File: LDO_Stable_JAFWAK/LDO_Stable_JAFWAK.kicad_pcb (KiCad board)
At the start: 4 copper layers, 96.5 x 51.1 mm, 79 parts, among them J1 VDD_SEL, J10 Load Cell and Buffer, J11 GND, J12 GND, J13 AD_PINS, J2 EN_FG, J3 VIN_FG, J4 VS_BUFF, J5 VOUT, J6 EN_AIN_SEL, J7 VIN_DC, J8 EN_SEL, J9 VOUT_BUFF, Q1 FDV305N, Q2 FDV305N, Q3 FDV305N, Q4 FDV305N, Q5 FDV305N, U1 SU272AFJK_LDO, U2 BUF634AIDR, U3 TMP235A2DBZR, U4 BUF634AIDR, U5 FXLP34, U6 FXLP34

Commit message: Produced Gerbers
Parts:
- added G***: LOGO, TPS7A7001_Evaluation_Board_footprint_lib:Stanford_logo, F.Cu at (94.0, 105.2)
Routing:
- net INB: track 69.4 -> 70.3 mm
- added copper zone on B.Cu, net GND
- added copper zone on F.Cu, net GND
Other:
- board size 96.5 x 51.1 mm -> 98.8 x 51.1 mm
- board text added: "JAFWAK"
- board text added: "Joseph Khamisy"
- board text removed: "Joseph Khamiby"

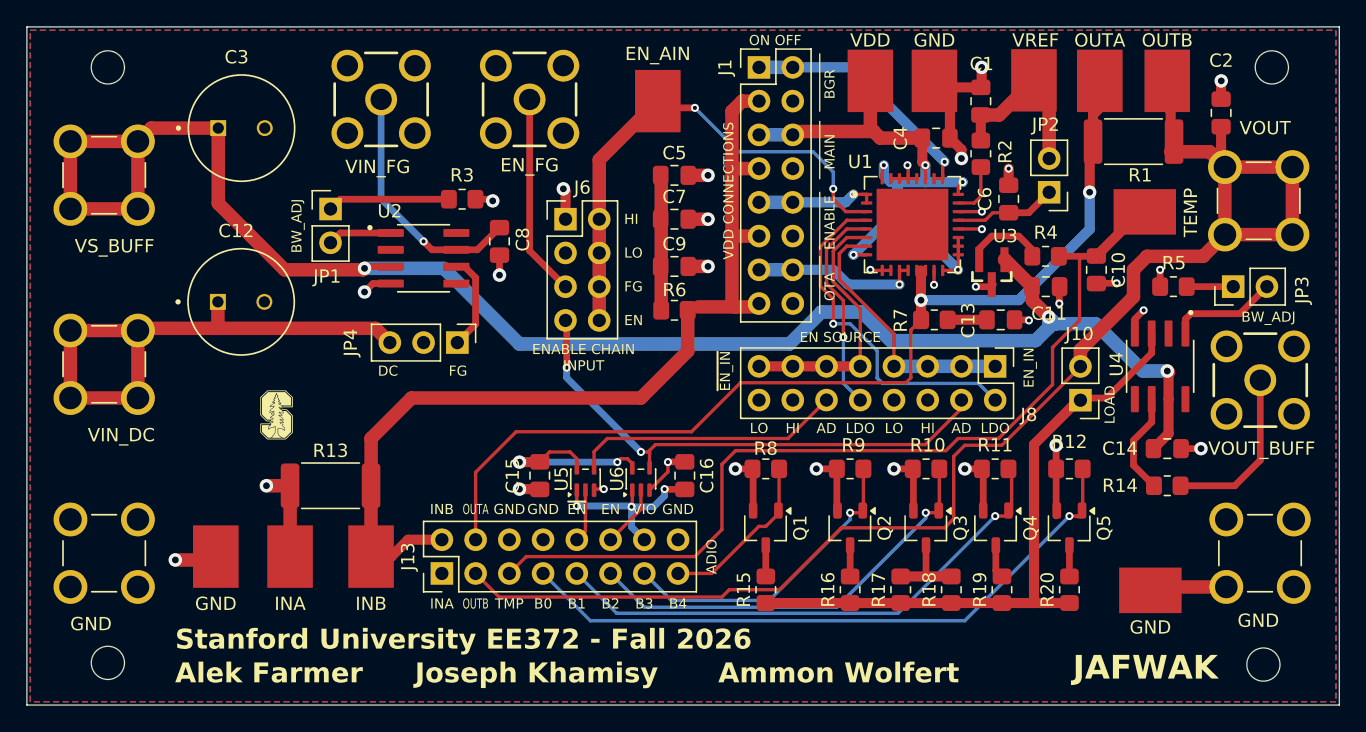
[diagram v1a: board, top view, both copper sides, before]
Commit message: Couple changes
More caps
Series Resitors
Stiching Vias
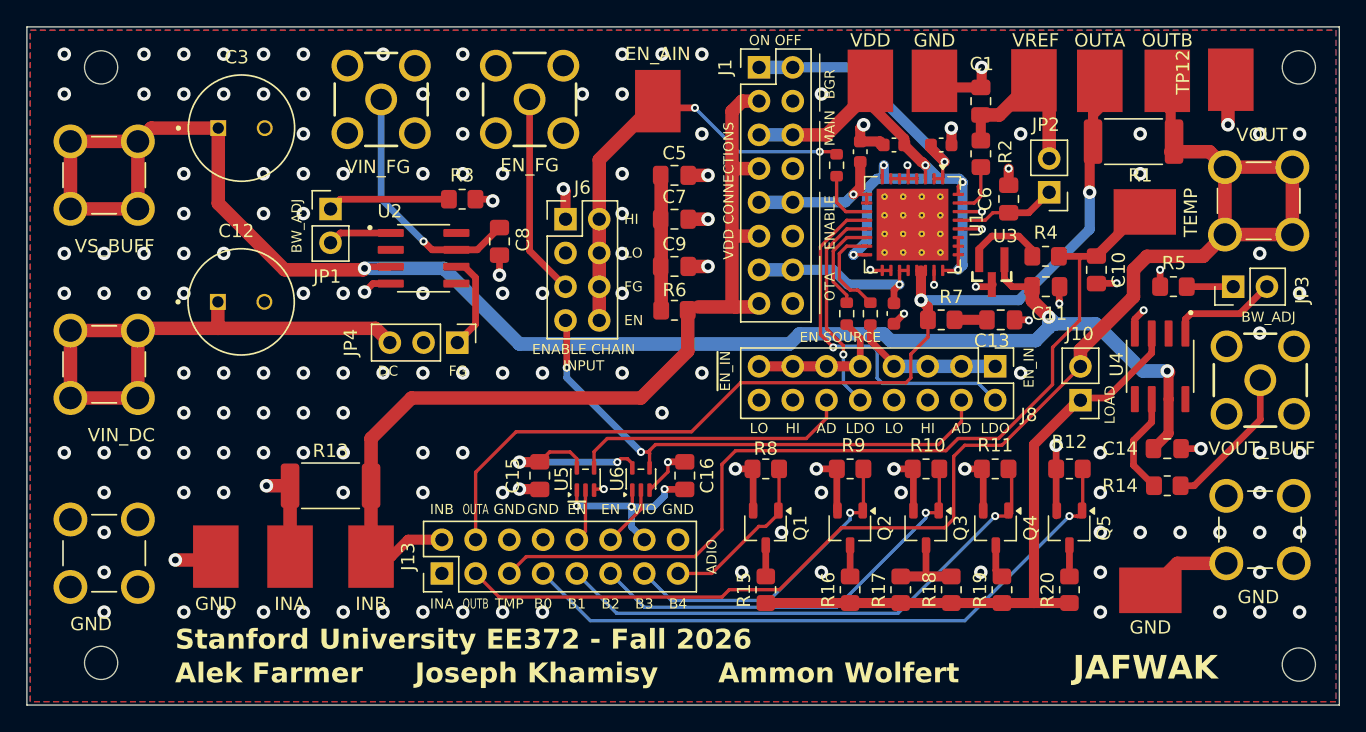
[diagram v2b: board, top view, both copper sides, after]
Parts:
- removed C2: 100n, Capacitor_SMD:C_0805_2012Metric_Pad1.18x1.45mm_HandSolder
- added C17: 100nF, Capacitor_SMD:C_0603_1608Metric, F.Cu at (144.0, 84.8)
- added C18: 100nF, Capacitor_SMD:C_0603_1608Metric, F.Cu at (137.9, 85.3)
- added C19: 100nF, Capacitor_SMD:C_0603_1608Metric, F.Cu at (140.5, 97.5)
- added R21: 1k, Resistor_SMD:R_0603_1608Metric, F.Cu at (138.7, 97.5)
- added R22: 1k, Resistor_SMD:R_0603_1608Metric, F.Cu at (136.9, 97.5)
- added R23: 1k, Resistor_SMD:R_0603_1608Metric, F.Cu at (136.1, 86.4)
- added TP12: GND, TPS7A7001_Evaluation_Board_footprint_lib:KEYSTONE_5016, F.Cu at (165.8, 79.9)
- C4: footprint Capacitor_SMD:C_0805_2012Metric_Pad1.18x1.45mm_HandSolder -> Capacitor_SMD:C_0603_1608Metric
- G***: moved to B.Cu
- U1: footprint Package_DFN_QFN:QFN-32-1EP_7x7mm_P0.65mm_EP5.4x5.4mm -> Package_DFN_QFN:QFN-32-1EP_7x7mm_P0.65mm_EP5.4x5.4mm_ThermalVias
- moved G*** 3.81 mm to (96.3, 102.1), turned to 180 degrees
- moved C4 3.22 mm to (140.5, 84.8), turned to 180 degrees
- moved H4 2.67 mm to (170.9, 124.0)
- moved H2 2.03 mm to (170.9, 79.0)
- moved J12 1.78 mm to (168.0, 113.8)
- moved R7 0.52 mm to (144.0, 98.0)
- moved H1 0.51 mm to (80.8, 79.0)
- moved H3 0.51 mm to (80.8, 123.8)
- turned U1 to -90 degrees
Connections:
- U1 pad 1: EN_VDD -> BGR_VDD
- U1 pad 10: GND -> EN_VDD
- U1 pad 11: OTA_VDD -> Net-(U1-EN_AIN)
- U1 pad 12: OTA_VDD -> /LDO Harness/EN_OUT
- U1 pad 13: OUTA -> /LDO Harness/~{EN_OUT}
- U1 pad 14: OUTA -> Net-(U1-~{EN_IN})
- U1 pad 15: GND -> Net-(U1-EN_IN)
- U1 pad 17: VDD -> GND
- U1 pad 18: VDD -> GND
- U1 pad 19: VDD -> OTA_VDD
- U1 pad 2: EN_VDD -> BGR_VDD
- U1 pad 20: GND -> OTA_VDD
- U1 pad 21: /LDO Harness/VREF_IN -> OUTA
- U1 pad 22: GND -> OUTA
- U1 pad 23: /LDO Harness/VREF_OUT -> GND
- U1 pad 25: BGR_VDD -> VDD
- U1 pad 26: BGR_VDD -> VDD
- U1 pad 29: GND -> /LDO Harness/VREF_IN
- U1 pad 3: /LDO Harness/EN_AIN -> VDD
- U1 pad 31: GND -> /LDO Harness/VREF_OUT
- U1 pad 33: /LDO Harness/EP -> (no net)
- U1 pad 4: /LDO Harness/EN_OUT -> GND
- U1 pad 5: /LDO Harness/~{EN_OUT} -> GND
- U1 pad 6: /LDO Harness/~{EN_IN} -> GND
- U1 pad 7: /LDO Harness/EN_IN -> GND
- U1 pad 9: GND -> EN_VDD
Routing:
- net /LDO Harness/~{EN_IN}: track 20.1 -> 11.2 mm
- net /LDO Harness/EN_IN: track 20.1 -> 11.9 mm
- net Net-(U1-EN_IN): track 0.00 -> 7.29 mm
- net Net-(U1-~{EN_IN}): track 0.00 -> 7.24 mm
- net VDD: track 54.8 -> 49.0 mm
- net /LDO Harness/EN_AIN: track 38.7 -> 33.5 mm
- net Net-(U1-EN_AIN): track 0.00 -> 4.77 mm
- net VOUT: track 108.7 -> 105.9 mm
- net EN_VDD: track 9.00 -> 11.6 mm
- net GND: track 83.3 -> 85.3 mm, vias 31 -> 165
- net Net-(J9-In): track 12.8 -> 11.0 mm
- net BGR_VDD: track 18.9 -> 20.6 mm
- net OTA_VDD: track 12.7 -> 14.3 mm
- net /LDO Harness/EN_OUT: track 26.3 -> 27.4 mm
- net /~{EN_CTRL_18}: track 20.3 -> 21.1 mm
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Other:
- board text added: "{ "ViaStitcher": "0.3.4", "GND Plane_1": { "HSpacing": "1", "VSpacing": "1", "HOffset": "0", "VOffset": "0", "Clearance": "0", "FillStyle": "Standard", "OnlyFilledCopper": true } }"
- board text added: "{ "ViaStitcher": "0.3.4", "GND Plane_1": { "HSpacing": "1", "VSpacing": "1", "HOffset": "0", "VOffset": "0", "Clearance": "4", "FillStyle": "Standard", "OnlyFilledCopper": true } }"
- board text added: "{ "ViaStitcher": "0.3.4", "GND Plane_1": { "HSpacing": "3", "VSpacing": "3", "HOffset": "0", "VOffset": "0", "Clearance": "0", "FillStyle": "Standard", "OnlyFilledCopper": true } }"

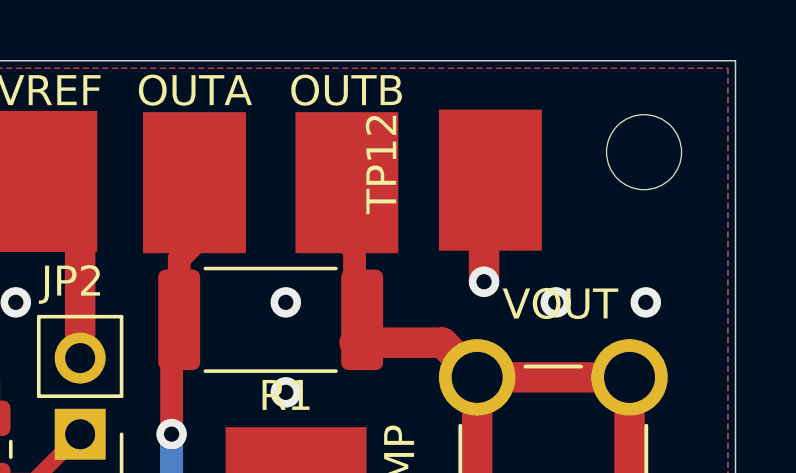
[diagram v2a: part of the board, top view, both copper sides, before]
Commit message: Added GND Label on a test point
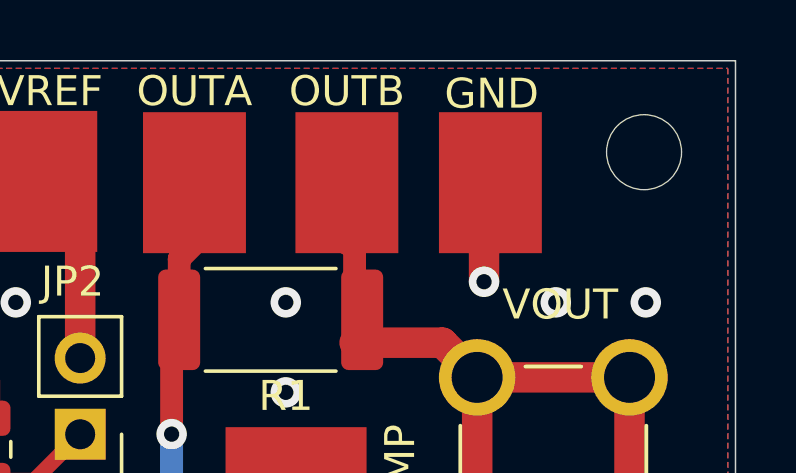
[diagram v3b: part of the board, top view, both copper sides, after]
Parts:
- moved TP12 0.09 mm to (165.8, 80.0)
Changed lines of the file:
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@@
 	(footprint "TPS7A7001_Evaluation_Board_footprint_lib:KEYSTONE_5016"
 		(layer "F.Cu")
-		(at 165.82 79.925 90)
+		(at 165.82 80.01 90)
 		(property "Reference" "TP12"
 			(at 0.575 -3.6 90)
 			(layer "F.SilkS")
+			(hide yes)
 			(effects
 				(font
@@
 		)
 		(property "Value" "GND"
-			(at 5.655 3.6 90)
-			(layer "F.Fab")
+			(at 2.963 0.042 180)
+			(layer "F.SilkS")
 			(effects
 				(font
